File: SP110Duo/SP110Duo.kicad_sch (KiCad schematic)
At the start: 249 parts, among them SW1 RotaryEncoder_Switch, SW10 Switch w/LED, SW100 Switch w/LED, SW101 Switch w/LED, SW102 Switch w/LED, SW103 Switch w/LED, SW104 Switch w/LED, SW105 Switch w/LED, SW106 Switch w/LED, SW107 Switch w/LED, SW108 Switch w/LED, SW109 Switch w/LED, SW11 Switch w/LED, SW110 Switch w/LED, SW12 Switch w/LED, SW13 Switch w/LED, SW14 Switch w/LED, SW15 Switch w/LED, SW16 Switch w/LED, SW17 Switch w/LED, SW18 Switch w/LED, SW19 Switch w/LED, SW2 Switch w/LED, SW20 Switch w/LED, SW21 Switch w/LED, SW22 Switch w/LED, SW23 Switch w/LED, SW24 Switch w/LED, SW25 Switch w/LED, SW26 Switch w/LED, SW27 Switch w/LED, SW28 Switch w/LED, SW29 Switch w/LED, SW3 Switch w/LED, SW30 Switch w/LED, SW31 Switch w/LED, SW32 Switch w/LED, SW33 Switch w/LED, SW34 Switch w/LED, SW35 Switch w/LED, SW36 Switch w/LED, SW37 Switch w/LED, SW38 Switch w/LED, SW39 Switch w/LED, SW4 Switch w/LED, SW40 Switch w/LED, SW41 Switch w/LED, SW42 Switch w/LED, SW43 Switch w/LED, SW44 Switch w/LED, SW45 Switch w/LED, SW46 Switch w/LED, SW47 Switch w/LED, SW48 Switch w/LED, SW49 Switch w/LED, SW5 Switch w/LED, SW50 Switch w/LED, SW51 Switch w/LED, SW52 Switch w/LED, SW53 Switch w/LED, SW54 Switch w/LED, SW55 Switch w/LED, SW56 Switch w/LED, SW57 Switch w/LED, SW58 Switch w/LED, SW59 Switch w/LED, SW6 Switch w/LED, SW60 Switch w/LED, SW61 RotaryEncoder_Switch, SW62 Switch w/LED, SW63 Switch w/LED, SW64 Switch w/LED, SW65 Switch w/LED, SW66 Switch w/LED, SW67 Switch w/LED, SW68 Switch w/LED, SW69 Switch w/LED, SW7 Switch w/LED, SW70 Switch w/LED, SW71 Switch w/LED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

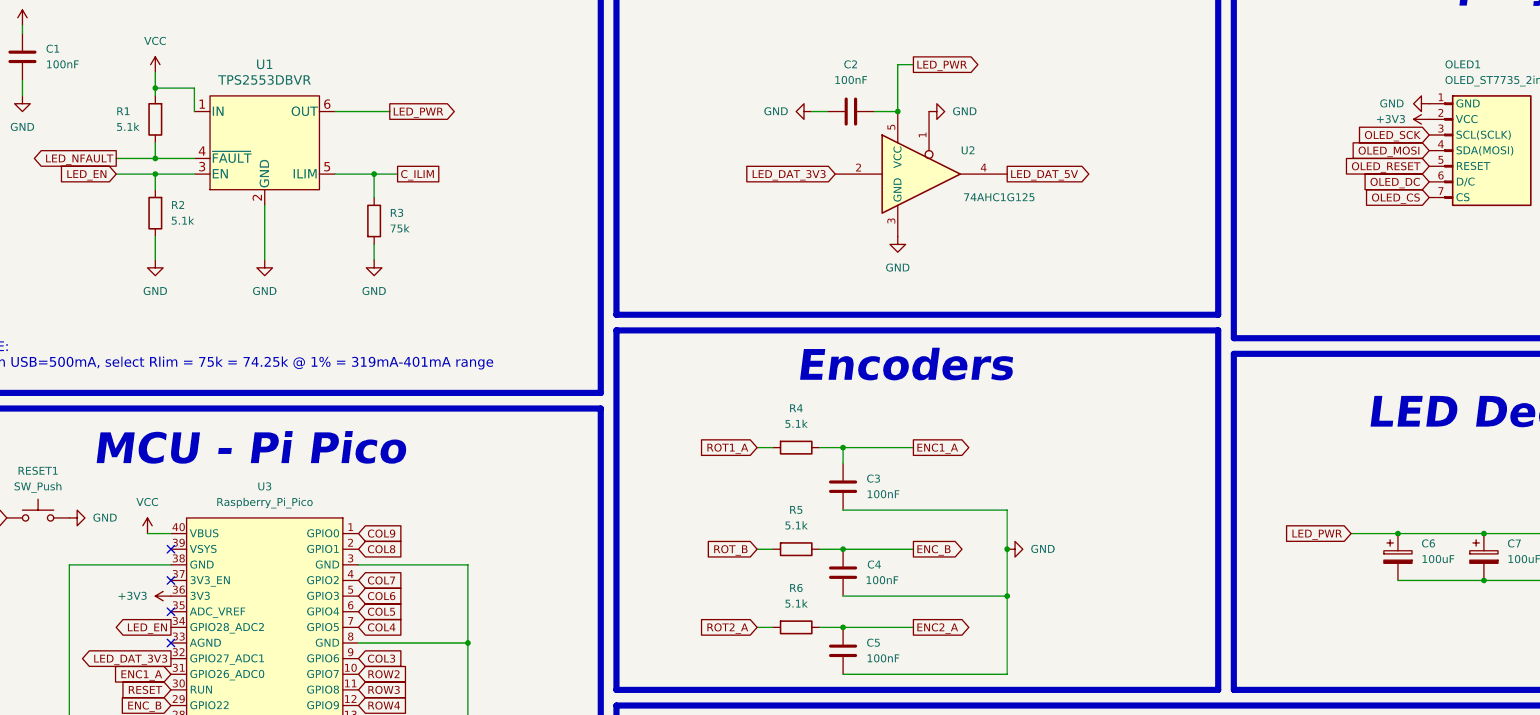
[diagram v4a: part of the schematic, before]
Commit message: Merge RGB EN and LCD VCC
Now RGB EN pin controls both RGB and LCD. This is due to lack of GPIO and a want to turn off the LCD when the keyboard goes to sleep.
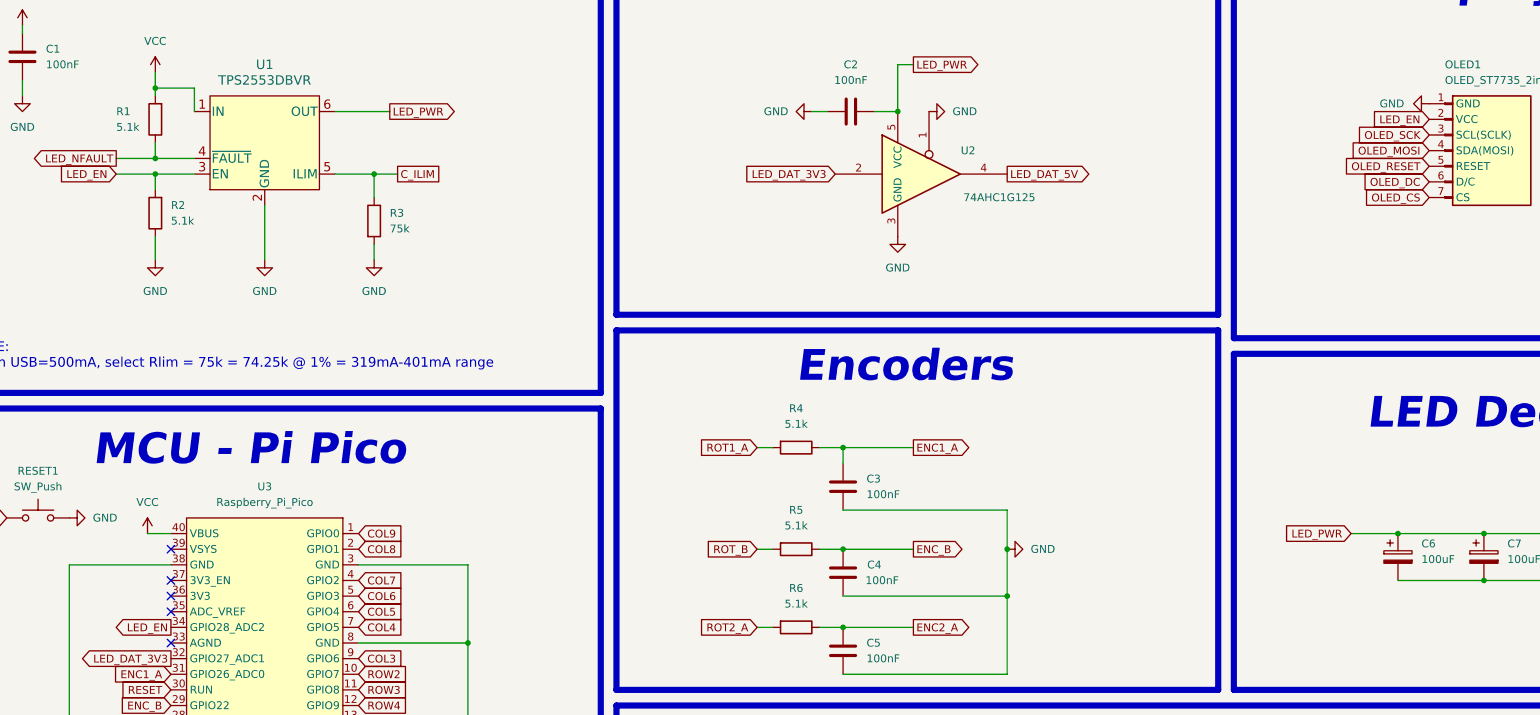
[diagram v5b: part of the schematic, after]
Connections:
- net LED_EN: now also OLED1.2 (VCC)
- net +3V3: no longer names the net of U3.36 (3V3)
- net +3V3: no longer OLED1.2 (VCC)
- no-connect marks 7 -> 8
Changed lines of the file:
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@@
   (no_connect (at 144.78 118.11))
   (no_connect (at 144.78 133.35))
+  (no_connect (at 144.78 125.73))
   (wire (pts (xy 576.58 288.29) (xy 601.98 288.29))
     (stroke (width 0) (type default))
@@
     )
   )
+  (global_label "LED_EN" (shape input) (at 349.25 48.26 180) (fields_autoplaced)
+    (effects (font (size 1.27 1.27)) (justify right))
+    (property "Intersheetrefs" "${INTERSHEET_REFS}" (at 339.3706 48.26 0)
+      (effects (font (size 1.27 1.27)) (justify right) hide)
+    )
+  )
   (global_label "COL5" (shape input) (at 436.88 215.9 90) (fields_autoplaced)
     (effects (font (size 1.27 1.27)) (justify left))
@@
     )
   )
-  (symbol (lib_id "power:+3V3") (at 144.78 125.73 90) (unit 1)
-    (in_bom yes) (on_board yes) (dnp no) (fields_autoplaced)
-    (property "Reference" "#PWR017" (at 148.59 125.73 0)
-      (effects (font (size 1.27 1.27)) hide)
-    )
-    (property "Value" "+3V3" (at 140.97 125.73 90)
-      (effects (font (size 1.27 1.27)) (justify left))
-    )
-    (property "Footprint" "" (at 144.78 125.73 0)
-      (effects (font (size 1.27 1.27)) hide)
-    )
-    (property "Datasheet" "" (at 144.78 125.73 0)
-      (effects (font (size 1.27 1.27)) hide)
-    )
-    (pin "1")
-    (instances
-      (project "SP110Duo"
-        (path "/9efe463e-e9e8-4c7d-9e2c-b657456ce19f"
-          (reference "#PWR017") (unit 1)
-        )
-      )
-    )
-  )
   (symbol (lib_id "KeebLib:Switch w/LED") (at 373.38 429.26 0) (unit 1)
     (in_bom yes) (on_board yes) (dnp no)
@@
         )
       )
-    )
-  )
-  (symbol (lib_id "power:+3V3") (at 349.25 48.26 90) (unit 1)
-    (in_bom yes) (on_board yes) (dnp no) (fields_autoplaced)
-    (property "Reference" "#PWR07" (at 353.06 48.26 0)
-      (effects (font (size 1.27 1.27)) hide)
-    )
-    (property "Value" "+3V3" (at 345.44 48.26 90)
-      (effects (font (size 1.27 1.27)) (justify left))
-    )
-    (property "Footprint" "" (at 349.25 48.26 0)
-      (effects (font (size 1.27 1.27)) hide)
-    )
-    (property "Datasheet" "" (at 349.25 48.26 0)
-      (effects (font (size 1.27 1.27)) hide)
-    )
-    (pin "1")
-    (instances
-      (project "SP110Duo"
-        (path "/9efe463e-e9e8-4c7d-9e2c-b657456ce19f"
-          (reference "#PWR07") (unit 1)
-        )
-      )

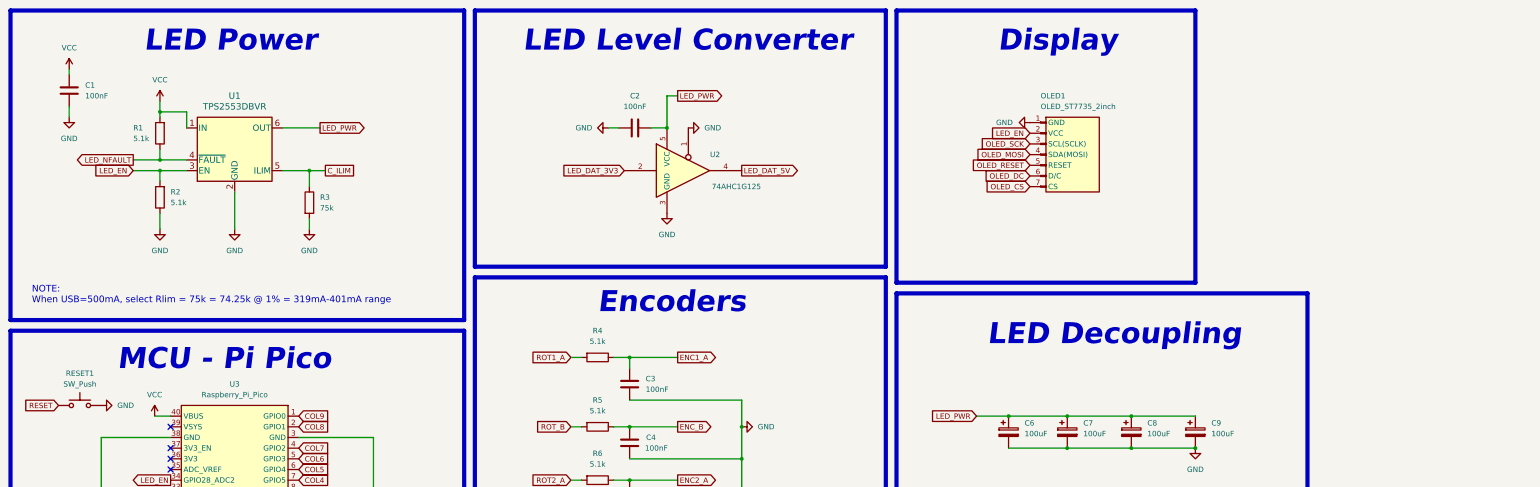
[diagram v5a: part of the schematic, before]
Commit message: Change LCD power to LED power signal
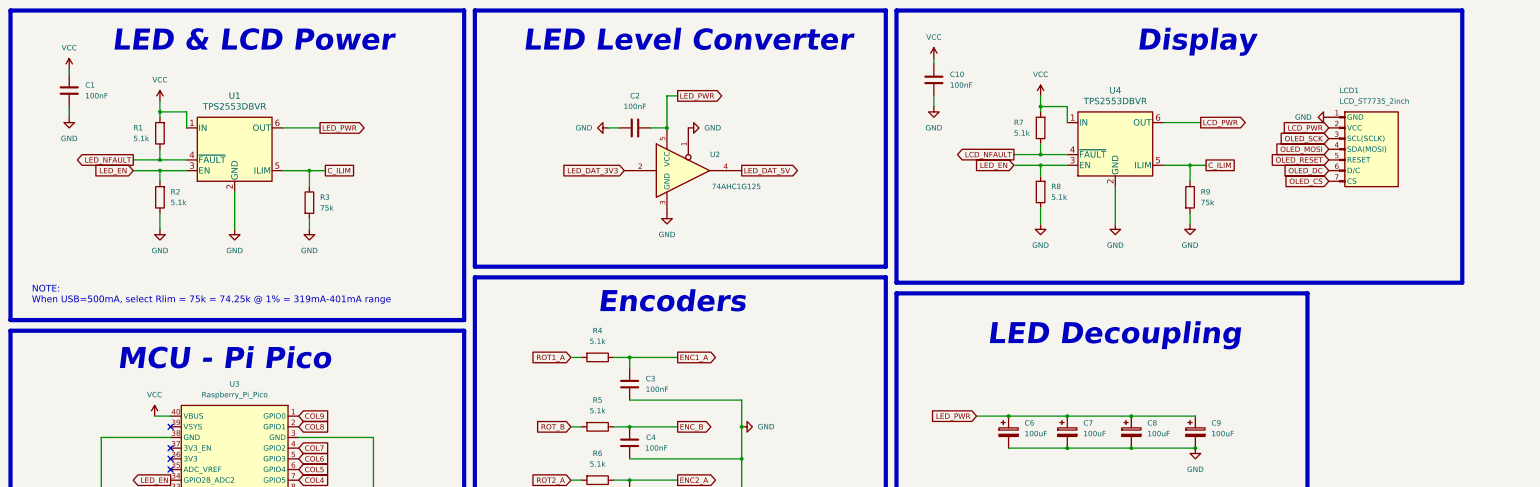
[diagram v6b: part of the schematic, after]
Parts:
- removed RESET1: SW_Push, KEEBIO:SW_SPST_TL3342, symbol Switch:SW_Push
- added C10: 100nF, Capacitor_SMD:C_1206_3216Metric_Pad1.33x1.80mm_HandSolder, symbol Device:C
- added R7, R8: 5.1k, Resistor_SMD:R_1206_3216Metric_Pad1.30x1.75mm_HandSolder, symbol Device:R
- added R9: 75k, Resistor_SMD:R_1206_3216Metric_Pad1.30x1.75mm_HandSolder, symbol Device:R
- added U4: TPS2553DBVR, Package_TO_SOT_SMD:SOT-23-6, symbol KeebLib:TPS2553DBVR
- LCD1: renamed from OLED1; value OLED_ST7735_2inch -> LCD_ST7735_2inch
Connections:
- net C_ILIM: now also R9.1, U4.5 (ILIM)
- net GND: now also C10.1, R8.1, R9.2, U4.2 (GND)
- net LED_EN: now also R8.2, U4.3 (EN); no longer LCD1.2 (VCC)
- net VCC: now also C10.2, R7.2, U4.1 (IN)
- new net LCD_NFAULT: R7.1, U4.4 (~{FAULT})
- new net LCD_PWR: LCD1.2 (VCC), U4.6 (OUT)
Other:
- note added: "LED & LCD Power"
- note removed: "LED Power"
- moved on the sheet: LCD1

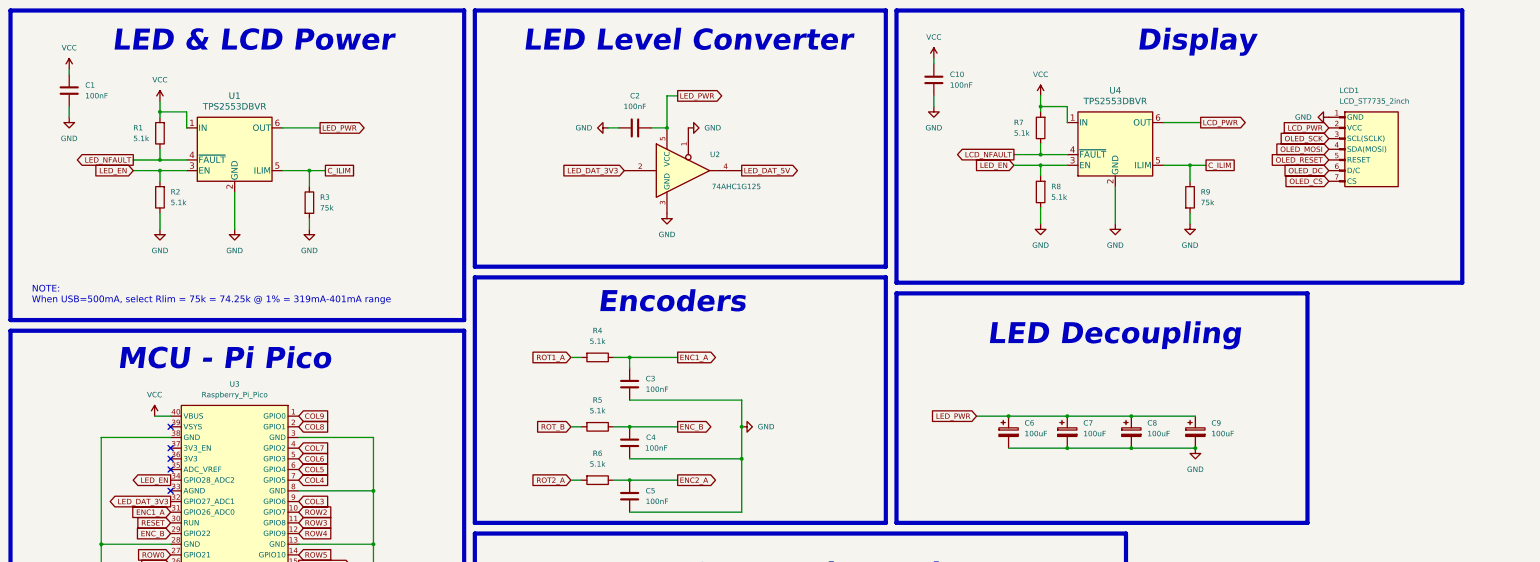
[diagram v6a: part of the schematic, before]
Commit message: Add RC delay for LED current limiter
Changing the GPIO for LED enable to only enable the LCD screen. Switching the current limiter enable to an RC delay circuit.
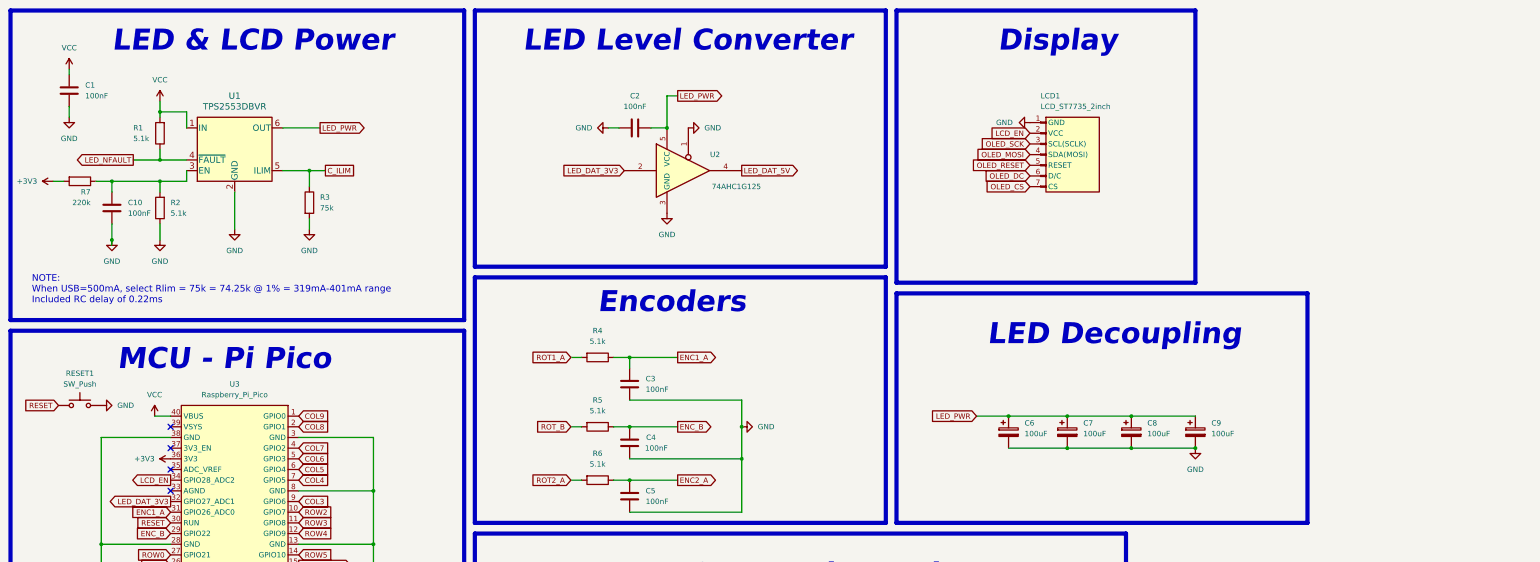
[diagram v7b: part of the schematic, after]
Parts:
- removed R8: 5.1k, Resistor_SMD:R_1206_3216Metric_Pad1.30x1.75mm_HandSolder, symbol Device:R
- removed R9: 75k, Resistor_SMD:R_1206_3216Metric_Pad1.30x1.75mm_HandSolder, symbol Device:R
- removed U4: TPS2553DBVR, Package_TO_SOT_SMD:SOT-23-6, symbol KeebLib:TPS2553DBVR
- added RESET1: SW_Push, KEEBIO:SW_SPST_TL3342, symbol Switch:SW_Push
- R7: value 5.1k -> 220k
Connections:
- net GND: now also RESET1.2
- net RESET: now also RESET1.1
- net VCC: no longer C10.2, R7.2
- net +3V3: now reaches U3.36 (3V3)
- net +3V3: now also R7.2
- net LCD_NFAULT: no longer names the net of R7.1
- net LCD_NFAULT: now also C10.2, R2.2, U1.3 (EN)
- net LCD_PWR renamed LCD_EN
- net LCD_EN: now also U3.34 (GPIO28_ADC2)
- removed net LED_EN: R2.2, U1.3 (EN), U3.34 (GPIO28_ADC2)
- no-connect marks 8 -> 7
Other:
- note added: "NOTE: When USB=500mA, select Rlim = 75k = 74.25k @ 1% = 319mA-401mA range Included RC delay of 0.22ms"
- note removed: "NOTE: When USB=500mA, select Rlim = 75k = 74.25k @ 1% = 319mA-401mA range"
- moved on the sheet: LCD1, R2

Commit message: update footprints
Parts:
- D1, D10, D100, D101, D102, D103, D104, D105, D106, D107, D108, D109, D11, D110, D12, D13, D14, D15, D16, D17, D18, D19, D2, D20, D21, D22, D23, D24, D25, D26, D27, D28, D29, D3, D30, D31, D32, D33, D34, D35, D36, D37, D38, D39, D4, D40, D41, D42, D43, D44, D45, D46, D47, D48, D49, D5, D50, D51, D52, D53, D54, D55, D56, D57, D58, D59, D6, D60, D61, D62, D63, D64, D65, D66, D67, D68, D69, D7, D70, D71, D72, D73, D74, D75, D76, D77, D78, D79, D8, D80, D81, D82, D83, D84, D85, D86, D87, D88, D89, D9, D90, D91, D92, D93, D94, D95, D96, D97, D98, D99: value Diode -> 1N4148W; footprint KEEBIO:Diode-Hybrid-Back -> KeebLib:SOD-123F; symbol ScottoKeebs:Placeholder_Diode -> Diode:1N4148W
- LCD1: value LCD_ST7735_2inch -> OLED_ST7735_2inch
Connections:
- net LED_EN: now reaches C10.2, R2.2, R7.1, U1.3 (EN)
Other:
- moved on the sheet: C1, C10, R1, R2, R3, R7, U1
